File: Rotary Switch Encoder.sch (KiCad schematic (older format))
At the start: 5 parts

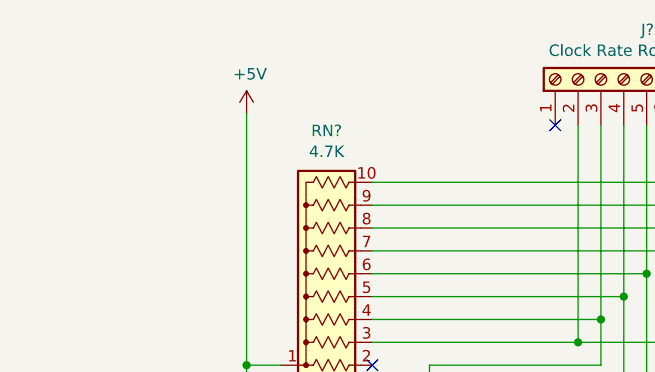
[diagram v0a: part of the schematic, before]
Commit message: Rotary Switch Encoder uses VCC power pin instead of +5V.
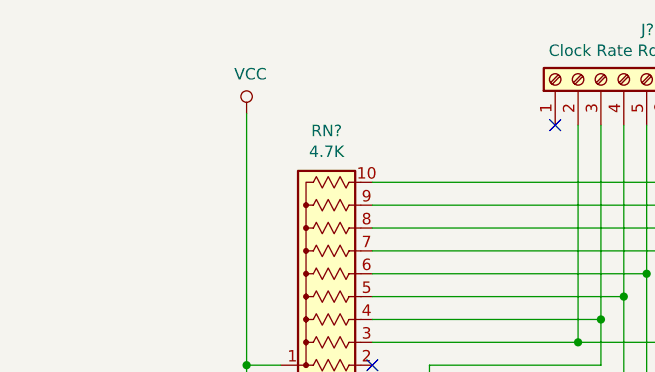
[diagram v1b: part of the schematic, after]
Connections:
- net +5V renamed VCC
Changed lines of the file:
@@
-	1    0    0    -1
-$EndComp
-$Comp
-L power:+5V #PWR?
-U 1 1 5D2B9D49
-P 3550 1500
-AR Path="/5D2B9D49" Ref="#PWR?"  Part="1"
-AR Path="/5D2A71D6/5D2B9D49" Ref="#PWR?"  Part="1"
-F 0 "#PWR?" H 3550 1350 50  0001 C CNN
-F 1 "+5V" H 3565 1673 50  0000 C CNN
-F 2 "" H 3550 1500 50  0001 C CNN
-F 3 "" H 3550 1500 50  0001 C CNN
-	1    3550 1500
 	1    0    0    -1
 $EndComp
@@
 	4100 2500 5000 2500
 Connection ~ 5000 2500
+$Comp
+L power:VCC #PWR?
+U 1 1 5D233769
+P 3550 1500
+F 0 "#PWR?" H 3550 1350 50  0001 C CNN
+F 1 "VCC" H 3567 1673 50  0000 C CNN
+F 2 "" H 3550 1500 50  0001 C CNN
+F 3 "" H 3550 1500 50  0001 C CNN
+	1    3550 1500
+	1    0    0    -1
+$EndComp
 $EndSCHEMATC
